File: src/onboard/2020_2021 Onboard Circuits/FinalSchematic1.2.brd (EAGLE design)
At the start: 137.6 x 80 mm, 83 parts, among them IC1 MIC2937A-5.0BT, IC3 A5975D

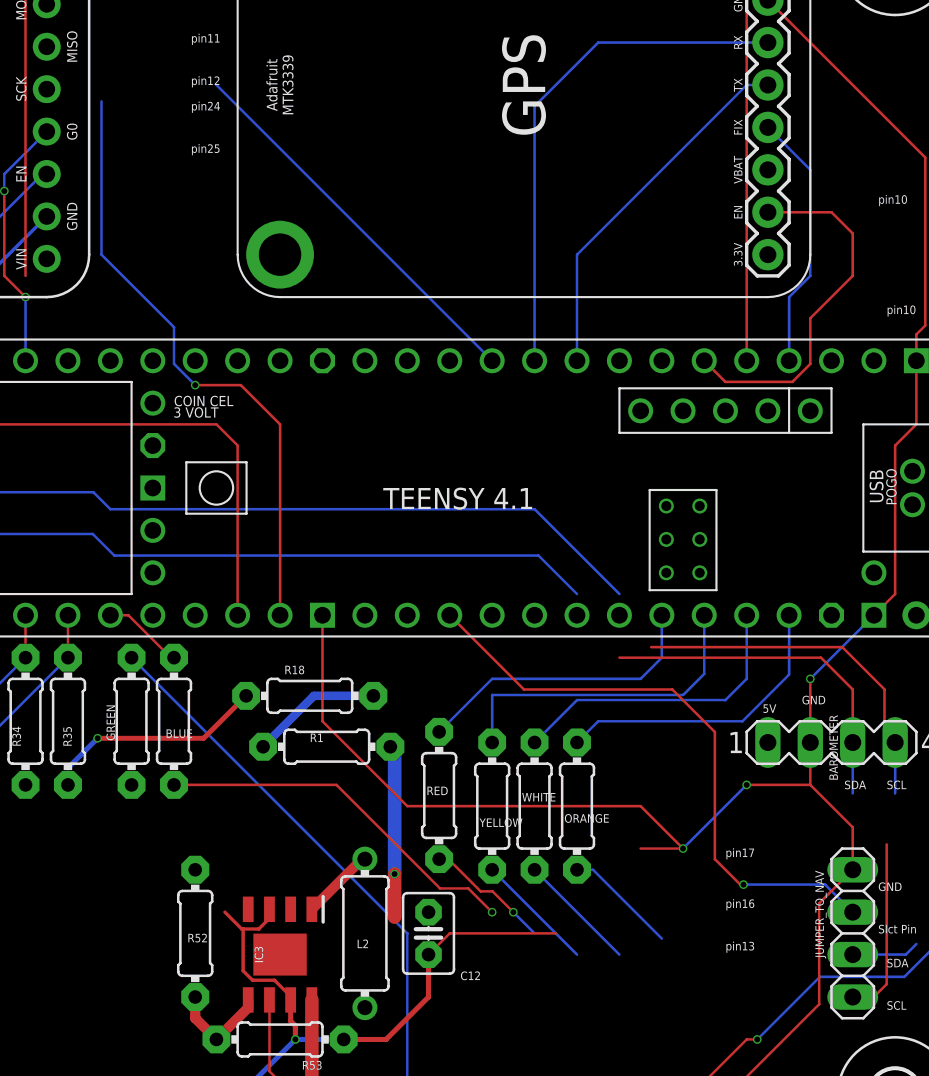
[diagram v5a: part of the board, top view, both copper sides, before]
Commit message: Formatting changes and 6v test point
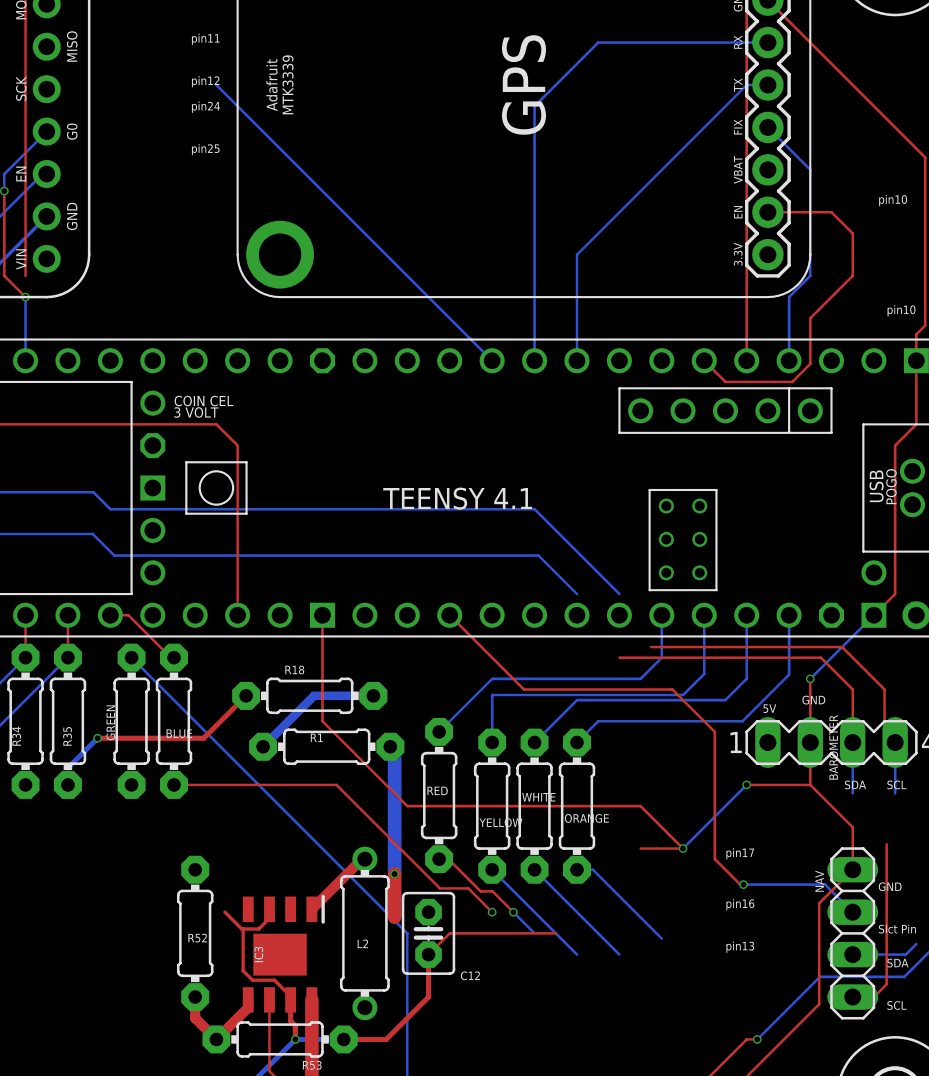
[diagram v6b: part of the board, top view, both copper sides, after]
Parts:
- renumbered JUMPER_TO_NAV to NAV
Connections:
- removed net MISO1: TEENSY4.1.41-A17/MISO1
- removed net N$5: TP5.TP
- net 6V: now also TP5.TP
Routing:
- net MISO1: track 36.8 -> 0.00 mm, vias 1 -> 0
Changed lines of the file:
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@@
 <attribute name="VALUE" x="65.3596" y="13.4366" size="0.508" layer="27" ratio="10" rot="R180"/>
 </element>
-<element name="JUMPER_TO_NAV" library="pinhead" library_urn="urn:adsk.eagle:library:325" package="1X04" package3d_urn="urn:adsk.eagle:package:22407/2" value="" x="93.98" y="15.24" smashed="yes" rot="R270">
+<element name="NAV" library="pinhead" library_urn="urn:adsk.eagle:library:325" package="1X04" package3d_urn="urn:adsk.eagle:package:22407/2" value="" x="93.98" y="15.24" smashed="yes" rot="R270">
 <attribute name="NAME" x="91.7448" y="18.9992" size="0.508" layer="25" ratio="10" rot="R270"/>
 <attribute name="POPULARITY" value="91" x="93.98" y="15.24" size="1.778" layer="27" rot="R270" display="off"/>
@@
 <wire x1="75.1666" y1="37.8634" x2="77.47" y2="35.56" width="0.1524" layer="16"/>
 <wire x1="49.7666" y1="37.8634" x2="75.1666" y2="37.8634" width="0.1524" layer="16"/>
-<contactref element="JUMPER_TO_NAV" pad="3"/>
+<contactref element="NAV" pad="3"/>
 <wire x1="93.98" y1="29.845" x2="93.98" y2="26.67" width="0.1524" layer="1"/>
 <wire x1="97.155" y1="13.97" x2="93.98" y2="13.97" width="0.1524" layer="16"/>
@@
 <wire x1="48.514" y1="41.656" x2="49.53" y2="40.64" width="0.1524" layer="16"/>
 <wire x1="49.53" y1="40.64" x2="74.93" y2="40.64" width="0.1524" layer="16"/>
-<contactref element="JUMPER_TO_NAV" pad="4"/>
+<contactref element="NAV" pad="4"/>
 <wire x1="96.012" y1="20.574" x2="96.012" y2="12.192" width="0.1524" layer="1"/>
 <wire x1="96.012" y1="12.192" x2="95.25" y2="11.43" width="0.1524" layer="1"/>
@@
 <wire x1="-10.16" y1="45.72" x2="-12.7" y2="41.91" width="0" layer="19" extent="1-1"/>
 <wire x1="-34.544" y1="-75.184" x2="-25.015" y2="38.972" width="0" layer="19" extent="1-1"/>
-</signal>
-<signal name="MISO1">
-<wire x1="48.9966" y1="65.0534" x2="48.9966" y2="55.88" width="0.1524" layer="16"/>
-<wire x1="48.9966" y1="55.88" x2="53.34" y2="51.5366" width="0.1524" layer="16"/>
-<wire x1="53.34" y1="49.33855" x2="54.61" y2="48.06855" width="0.1524" layer="16"/>
-<wire x1="53.34" y1="51.5366" x2="53.34" y2="49.33855" width="0.1524" layer="16"/>
-<contactref element="TEENSY4.1" pad="41-A17/MISO1"/>
-<wire x1="59.69" y1="34.29" x2="59.69" y2="45.72" width="0.1524" layer="1"/>
-<wire x1="59.69" y1="45.72" x2="57.34145" y2="48.06855" width="0.1524" layer="1"/>
-<wire x1="57.34145" y1="48.06855" x2="54.61" y2="48.06855" width="0.1524" layer="1"/>
-<via x="54.61" y="48.06855" extent="1-16" drill="0.35"/>
 </signal>
 <signal name="DIP2">
@@
 <contactref element="TEENSY4.1" pad="GND6"/>
 <wire x1="96.52" y1="35.56" x2="95.25" y2="34.29" width="0.1524" layer="1"/>
-<contactref element="JUMPER_TO_NAV" pad="1"/>
+<contactref element="NAV" pad="1"/>
 <wire x1="93.98" y1="21.59" x2="91.44" y2="24.13" width="0.1524" layer="1"/>
 <wire x1="91.44" y1="24.13" x2="91.44" y2="26.67" width="0.1524" layer="1"/>
@@
 </signal>
 <signal name="SELECT_PIN">
-<contactref element="JUMPER_TO_NAV" pad="2"/>
+<contactref element="NAV" pad="2"/>
 <contactref element="TEENSY4.1" pad="15-A1/RX3/SPDIF_IN"/>
 <wire x1="87.249" y1="18.161" x2="85.725" y2="19.685" width="0.1524" layer="1"/>
@@
 <wire x1="58.42" y1="2.54" x2="-30.988" y2="-61.468" width="0" layer="19" extent="1-1"/>
 </signal>
-<signal name="N$5">
-<contactref element="TP5" pad="TP"/>
-</signal>
 <signal name="6V">
 <contactref element="6V_PWR" pad="1"/>
 <contactref element="6V_PWR" pad="2"/>
 <contactref element="IC1" pad="1"/>
-<wire x1="-33.528" y1="-50.292" x2="-32.512" y2="-93.98" width="0" layer="19" extent="1-1"/>
+<contactref element="TP5" pad="TP"/>
+<wire x1="-34.544" y1="-84.328" x2="-32.512" y2="-93.98" width="0" layer="19" extent="1-1"/>
+<wire x1="-33.528" y1="-50.292" x2="-34.544" y2="-84.328" width="0" layer="19" extent="1-1"/>
 <wire x1="-30.988" y1="-50.292" x2="-33.528" y2="-50.292" width="0" layer="19" extent="1-1"/>
 </signal>

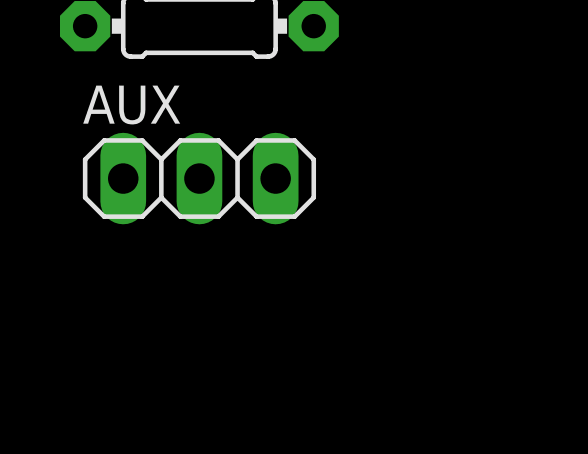
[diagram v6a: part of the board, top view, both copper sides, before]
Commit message: Added bulk decoupling
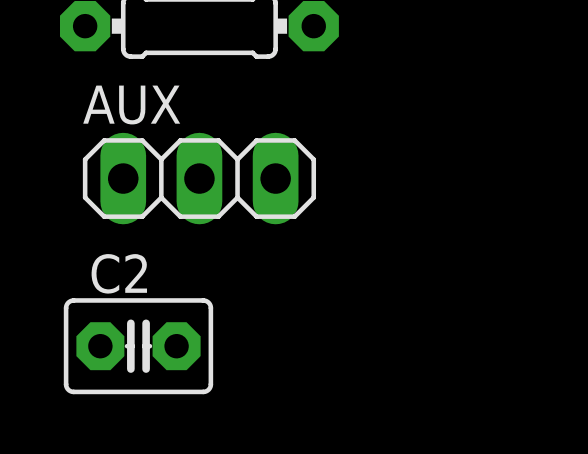
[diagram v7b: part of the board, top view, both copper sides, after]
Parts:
- added C2: 10uF, capacitor-wima:C2.5-3
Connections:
- net 5V: now also C2.1
- net GND: now also C2.2
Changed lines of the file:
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@@
 <attribute name="VALUE" x="-34.798" y="-118.491" size="1.27" layer="27"/>
+</element>
+<element name="C2" library="capacitor-wima" library_urn="urn:adsk.eagle:library:116" package="C2.5-3" package3d_urn="urn:adsk.eagle:package:5436/1" value="10uF" x="-33.02" y="-120.904" smashed="yes">
+<attribute name="NAME" x="-34.671" y="-119.126" size="1.27" layer="25" ratio="10"/>
+<attribute name="POPULARITY" value="38" x="-33.02" y="-120.904" size="1.778" layer="27" display="off"/>
+<attribute name="VALUE" x="-34.671" y="-123.952" size="1.27" layer="27" ratio="10"/>
 </element>
 </elements>
@@
 <contactref element="IC1" pad="3"/>
 <contactref element="C1" pad="1"/>
+<contactref element="C2" pad="1"/>
 <wire x1="97.79" y1="34.29" x2="88.9" y2="73.66" width="0" layer="19" extent="1-1"/>
 <wire x1="88.9" y1="26.67" x2="97.79" y2="34.29" width="0" layer="19" extent="1-1"/>
@@
 <wire x1="-27.432" y1="-93.98" x2="-30.988" y2="-89.408" width="0" layer="19" extent="1-1"/>
 <wire x1="-34.29" y1="-103.632" x2="-27.432" y2="-93.98" width="0" layer="19" extent="1-1"/>
+<wire x1="-34.29" y1="-120.904" x2="-34.29" y2="-103.632" width="0" layer="19" extent="1-1"/>
 </signal>
 <signal name="DIP1">
@@
 <contactref element="R23" pad="1"/>
 <contactref element="AUX" pad="1"/>
+<contactref element="C2" pad="2"/>
+<wire x1="-33.528" y1="-115.316" x2="-31.75" y2="-120.904" width="0" layer="19" extent="1-1"/>
 <wire x1="-34.798" y1="-110.236" x2="-33.528" y2="-115.316" width="0" layer="19" extent="1-1"/>
 <wire x1="-29.972" y1="-93.98" x2="-34.798" y2="-110.236" width="0" layer="19" extent="1-1"/>

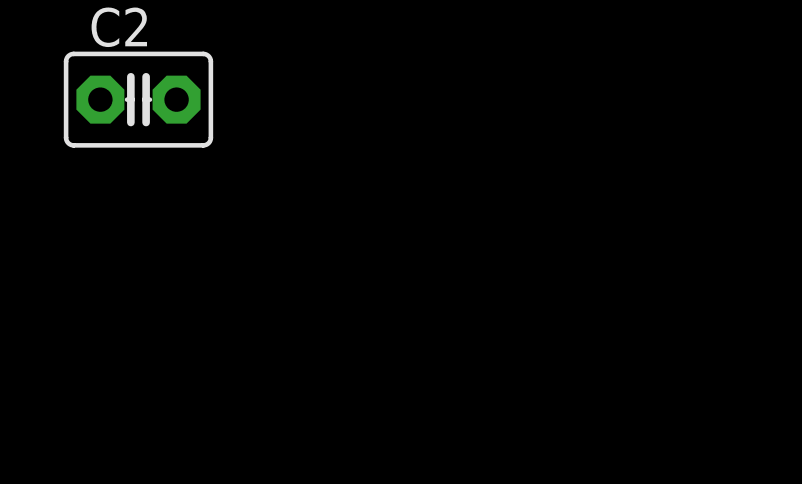
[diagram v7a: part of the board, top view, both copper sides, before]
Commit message: Added BMP280 I2C Part
Added to SCH sheet 4
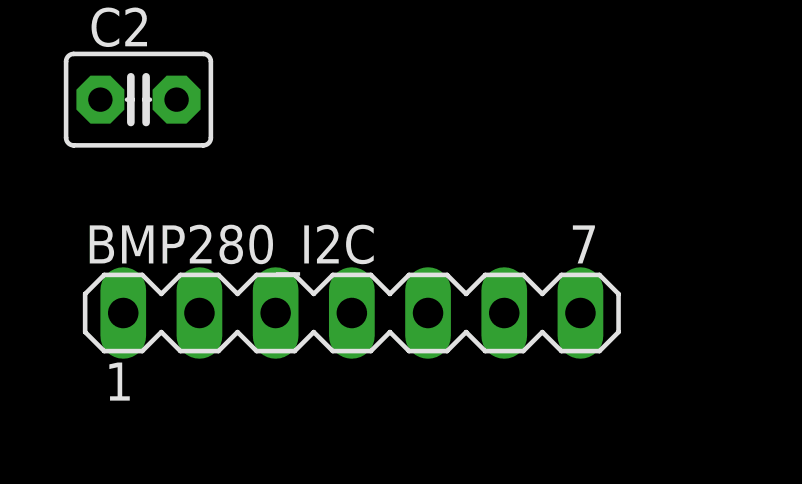
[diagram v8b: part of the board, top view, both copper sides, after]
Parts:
- added BMP280_I2C: (no value), con-lstb:MA07-1
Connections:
- new net 3V0: BMP280_I2C.2
- new net CS: BMP280_I2C.7
- new net SCK: BMP280_I2C.4
- new net SDI: BMP280_I2C.6
- new net SDO: BMP280_I2C.5
- new net VIN: BMP280_I2C.1
- net GND: now also BMP280_I2C.3
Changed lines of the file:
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@@
 <attribute name="VALUE" x="-34.671" y="-123.952" size="1.27" layer="27" ratio="10"/>
+</element>
+<element name="BMP280_I2C" library="con-lstb" library_urn="urn:adsk.eagle:library:162" package="MA07-1" package3d_urn="urn:adsk.eagle:package:8341/1" value="" x="-25.908" y="-128.016" smashed="yes">
+<attribute name="MF" value="" x="-25.908" y="-128.016" size="1.778" layer="27" display="off"/>
+<attribute name="MPN" value="" x="-25.908" y="-128.016" size="1.778" layer="27" display="off"/>
+<attribute name="NAME" x="-34.798" y="-126.365" size="1.27" layer="25" ratio="10"/>
+<attribute name="OC_FARNELL" value="unknown" x="-25.908" y="-128.016" size="1.778" layer="27" display="off"/>
+<attribute name="OC_NEWARK" value="unknown" x="-25.908" y="-128.016" size="1.778" layer="27" display="off"/>
+<attribute name="POPULARITY" value="4" x="-25.908" y="-128.016" size="1.778" layer="27" display="off"/>
+<attribute name="VALUE" x="-28.448" y="-130.937" size="1.27" layer="27" ratio="10"/>
 </element>
 </elements>
@@
 <contactref element="AUX" pad="1"/>
 <contactref element="C2" pad="2"/>
+<contactref element="BMP280_I2C" pad="3"/>
+<wire x1="-31.75" y1="-120.904" x2="-28.448" y2="-128.016" width="0" layer="19" extent="1-1"/>
 <wire x1="-33.528" y1="-115.316" x2="-31.75" y2="-120.904" width="0" layer="19" extent="1-1"/>
 <wire x1="-34.798" y1="-110.236" x2="-33.528" y2="-115.316" width="0" layer="19" extent="1-1"/>
@@
 <wire x1="52.07" y1="49.53" x2="-28.448" y2="-115.316" width="0" layer="19" extent="1-1"/>
 </signal>
+<signal name="VIN">
+<contactref element="BMP280_I2C" pad="1"/>
+</signal>
+<signal name="3V0">
+<contactref element="BMP280_I2C" pad="2"/>
+</signal>
+<signal name="SCK">
+<contactref element="BMP280_I2C" pad="4"/>
+</signal>
+<signal name="SDO">
+<contactref element="BMP280_I2C" pad="5"/>
+</signal>
+<signal name="SDI">
+<contactref element="BMP280_I2C" pad="6"/>
+</signal>
+<signal name="CS">
+<contactref element="BMP280_I2C" pad="7"/>
+</signal>
 </signals>
